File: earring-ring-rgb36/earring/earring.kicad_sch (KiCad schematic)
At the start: 44 parts, among them J1 Conn_01x04, SW1 SW_Push, U2 STM32L031G6Ux

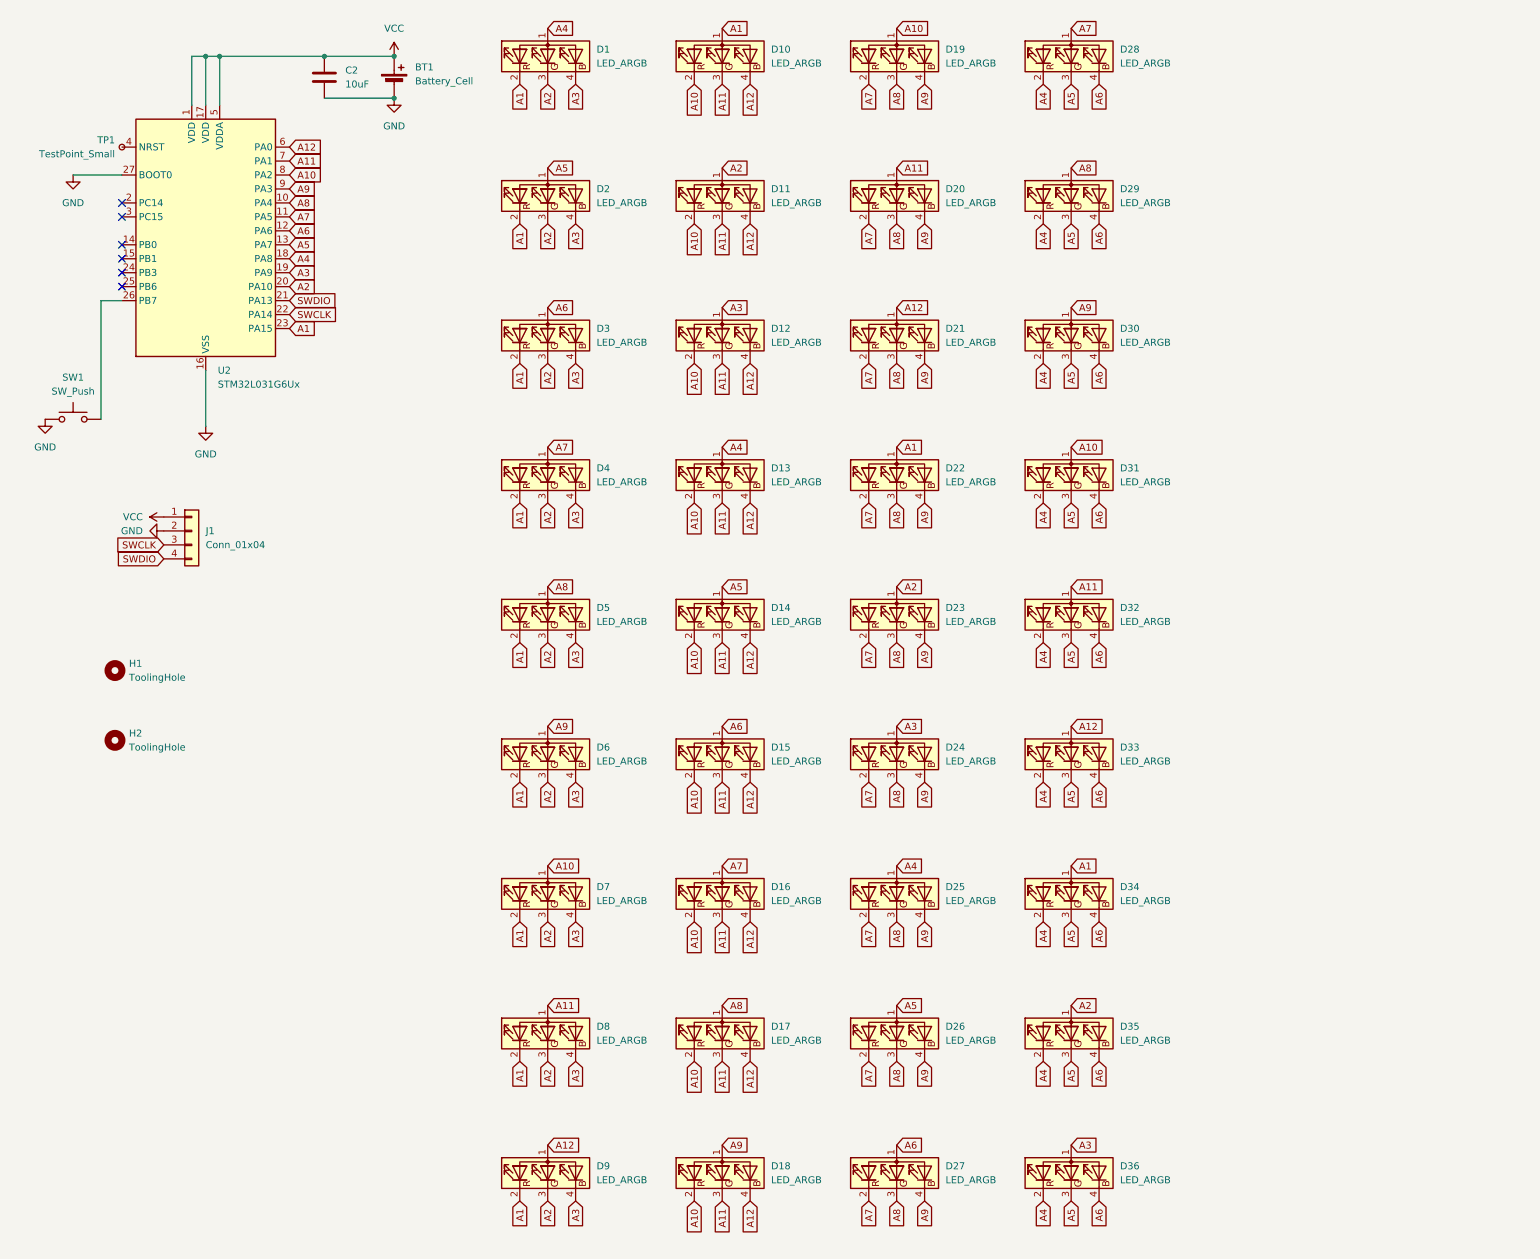
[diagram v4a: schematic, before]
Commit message: earring-ring-rgb36: updated PCB in many ways
 - updated to KiCad 9
 - added resistors for the LEDs (now assuming individual charlieplexing)
 - added MOSFET for reverse current protection
 - redid most of the wiring on the PCB, with the addition of the
   resistors
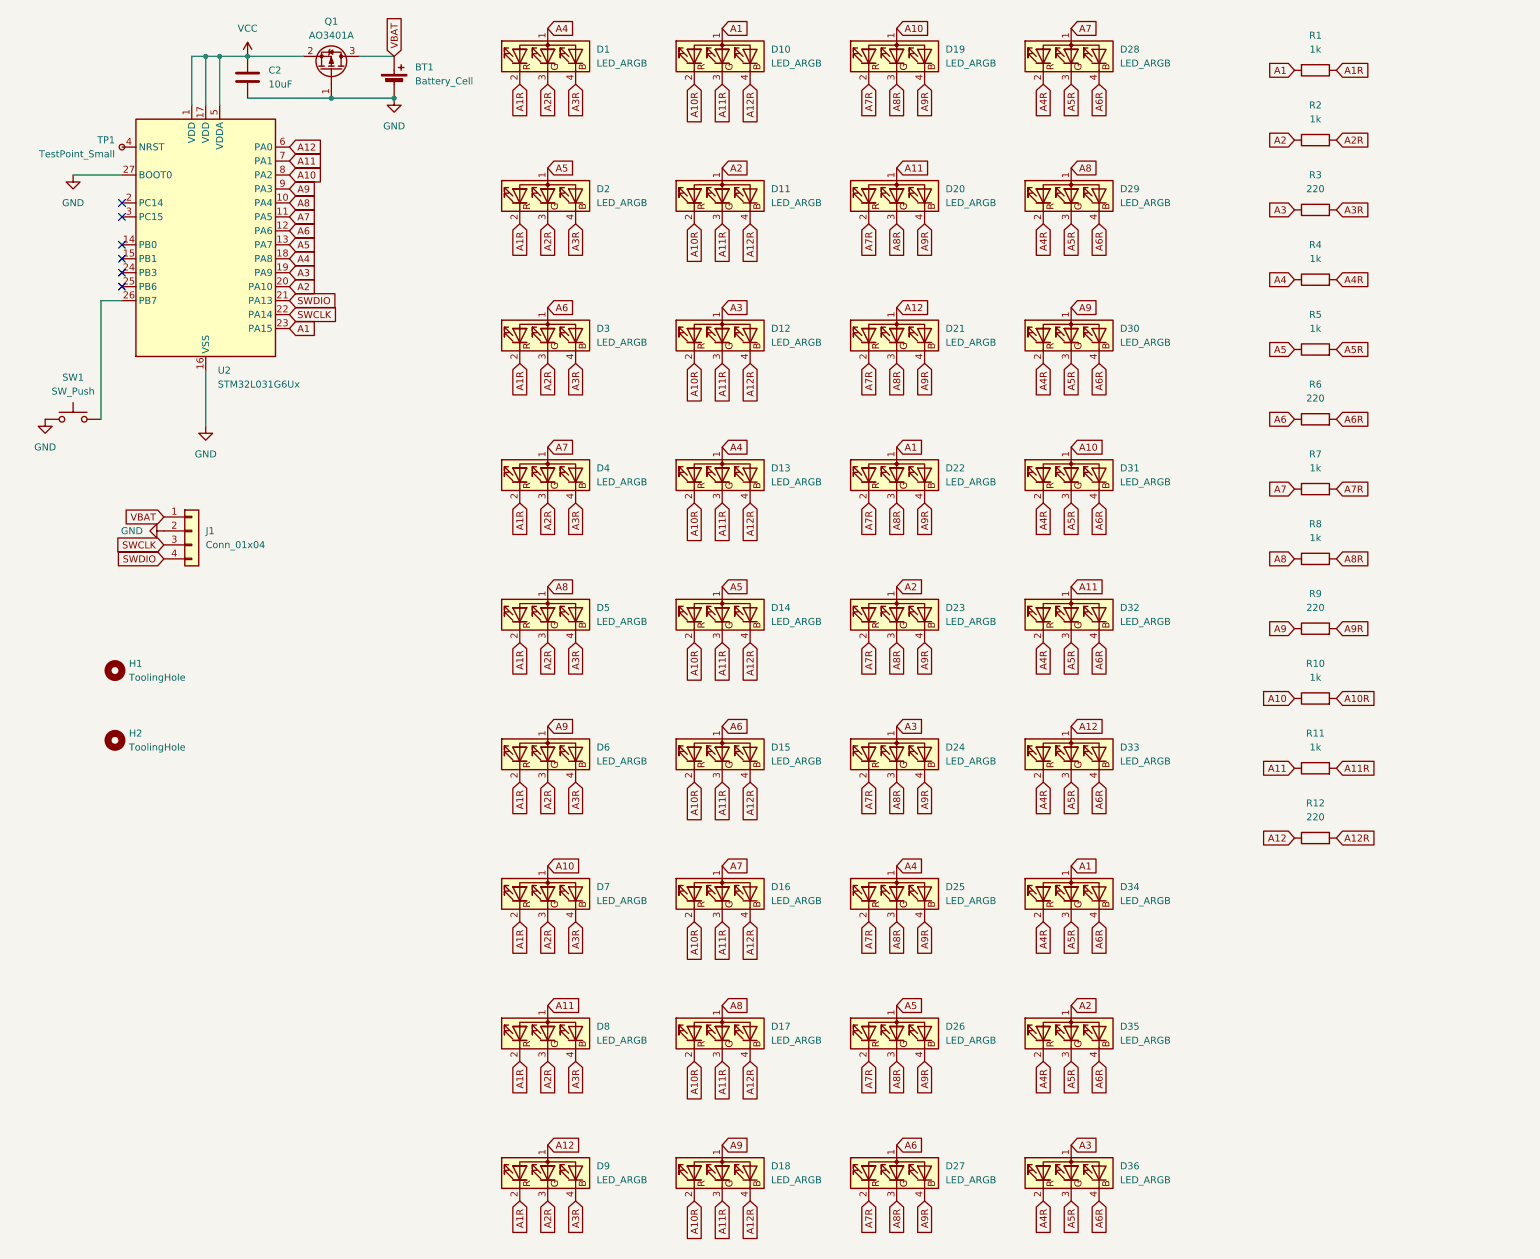
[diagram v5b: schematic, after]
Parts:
- added Q1: AO3401A, Package_TO_SOT_SMD:SOT-23, symbol Transistor_FET:AO3401A
- added R1, R10, R11, R2, R4, R5, R7, R8: 1k, Resistor_SMD:R_0402_1005Metric, symbol Device:R
- added R12, R3, R6, R9: 220, Resistor_SMD:R_0402_1005Metric, symbol Device:R
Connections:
- net A1: now also R1.2; no longer D1.2 (RK), D2.2 (RK), D3.2 (RK), D4.2 (RK), D5.2 (RK), D6.2 (RK), D7.2 (RK), D8.2 (RK), D9.2 (RK)
- net A10: now also R10.1; no longer D10.2 (RK), D11.2 (RK), D12.2 (RK), D13.2 (RK), D14.2 (RK), D15.2 (RK), D16.2 (RK), D17.2 (RK), D18.2 (RK)
- net A11: now also R11.1; no longer D10.3 (GK), D11.3 (GK), D12.3 (GK), D13.3 (GK), D14.3 (GK), D15.3 (GK), D16.3 (GK), D17.3 (GK), D18.3 (GK)
- net A12: now also R12.1; no longer D10.4 (BK), D11.4 (BK), D12.4 (BK), D13.4 (BK), D14.4 (BK), D15.4 (BK), D16.4 (BK), D17.4 (BK), D18.4 (BK)
- net A2: now also R2.1; no longer D1.3 (GK), D2.3 (GK), D3.3 (GK), D4.3 (GK), D5.3 (GK), D6.3 (GK), D7.3 (GK), D8.3 (GK), D9.3 (GK)
- net A3: now also R3.1; no longer D1.4 (BK), D2.4 (BK), D3.4 (BK), D4.4 (BK), D5.4 (BK), D6.4 (BK), D7.4 (BK), D8.4 (BK), D9.4 (BK)
- net A4: now also R4.1; no longer D28.2 (RK), D29.2 (RK), D30.2 (RK), D31.2 (RK), D32.2 (RK), D33.2 (RK), D34.2 (RK), D35.2 (RK), D36.2 (RK)
- net A5: now also R5.1; no longer D28.3 (GK), D29.3 (GK), D30.3 (GK), D31.3 (GK), D32.3 (GK), D33.3 (GK), D34.3 (GK), D35.3 (GK), D36.3 (GK)
- net A6: now also R6.1; no longer D28.4 (BK), D29.4 (BK), D30.4 (BK), D31.4 (BK), D32.4 (BK), D33.4 (BK), D34.4 (BK), D35.4 (BK), D36.4 (BK)
- net A7: now also R7.1; no longer D19.2 (RK), D20.2 (RK), D21.2 (RK), D22.2 (RK), D23.2 (RK), D24.2 (RK), D25.2 (RK), D26.2 (RK), D27.2 (RK)
- net A8: now also R8.1; no longer D19.3 (GK), D20.3 (GK), D21.3 (GK), D22.3 (GK), D23.3 (GK), D24.3 (GK), D25.3 (GK), D26.3 (GK), D27.3 (GK)
- net A9: now also R9.1; no longer D19.4 (BK), D20.4 (BK), D21.4 (BK), D22.4 (BK), D23.4 (BK), D24.4 (BK), D25.4 (BK), D26.4 (BK), D27.4 (BK)
- net GND: now also Q1.1 (G)
- net VCC: now also Q1.2 (S); no longer BT1.1 (+), J1.1 (Pin_1)
- new net A10R: D10.2 (RK), D11.2 (RK), D12.2 (RK), D13.2 (RK), D14.2 (RK), D15.2 (RK), D16.2 (RK), D17.2 (RK), D18.2 (RK), R10.2
- new net A11R: D10.3 (GK), D11.3 (GK), D12.3 (GK), D13.3 (GK), D14.3 (GK), D15.3 (GK), D16.3 (GK), D17.3 (GK), D18.3 (GK), R11.2
- new net A12R: D10.4 (BK), D11.4 (BK), D12.4 (BK), D13.4 (BK), D14.4 (BK), D15.4 (BK), D16.4 (BK), D17.4 (BK), D18.4 (BK), R12.2
- new net A1R: D1.2 (RK), D2.2 (RK), D3.2 (RK), D4.2 (RK), D5.2 (RK), D6.2 (RK), D7.2 (RK), D8.2 (RK), D9.2 (RK), R1.1
- new net A2R: D1.3 (GK), D2.3 (GK), D3.3 (GK), D4.3 (GK), D5.3 (GK), D6.3 (GK), D7.3 (GK), D8.3 (GK), D9.3 (GK), R2.2
- new net A3R: D1.4 (BK), D2.4 (BK), D3.4 (BK), D4.4 (BK), D5.4 (BK), D6.4 (BK), D7.4 (BK), D8.4 (BK), D9.4 (BK), R3.2
- new net A4R: D28.2 (RK), D29.2 (RK), D30.2 (RK), D31.2 (RK), D32.2 (RK), D33.2 (RK), D34.2 (RK), D35.2 (RK), D36.2 (RK), R4.2
- new net A5R: D28.3 (GK), D29.3 (GK), D30.3 (GK), D31.3 (GK), D32.3 (GK), D33.3 (GK), D34.3 (GK), D35.3 (GK), D36.3 (GK), R5.2
- new net A6R: D28.4 (BK), D29.4 (BK), D30.4 (BK), D31.4 (BK), D32.4 (BK), D33.4 (BK), D34.4 (BK), D35.4 (BK), D36.4 (BK), R6.2
- new net A7R: D19.2 (RK), D20.2 (RK), D21.2 (RK), D22.2 (RK), D23.2 (RK), D24.2 (RK), D25.2 (RK), D26.2 (RK), D27.2 (RK), R7.2
- new net A8R: D19.3 (GK), D20.3 (GK), D21.3 (GK), D22.3 (GK), D23.3 (GK), D24.3 (GK), D25.3 (GK), D26.3 (GK), D27.3 (GK), R8.2
- new net A9R: D19.4 (BK), D20.4 (BK), D21.4 (BK), D22.4 (BK), D23.4 (BK), D24.4 (BK), D25.4 (BK), D26.4 (BK), D27.4 (BK), R9.2
- new net VBAT: BT1.1 (+), J1.1 (Pin_1), Q1.3 (D)
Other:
- moved on the sheet: C2

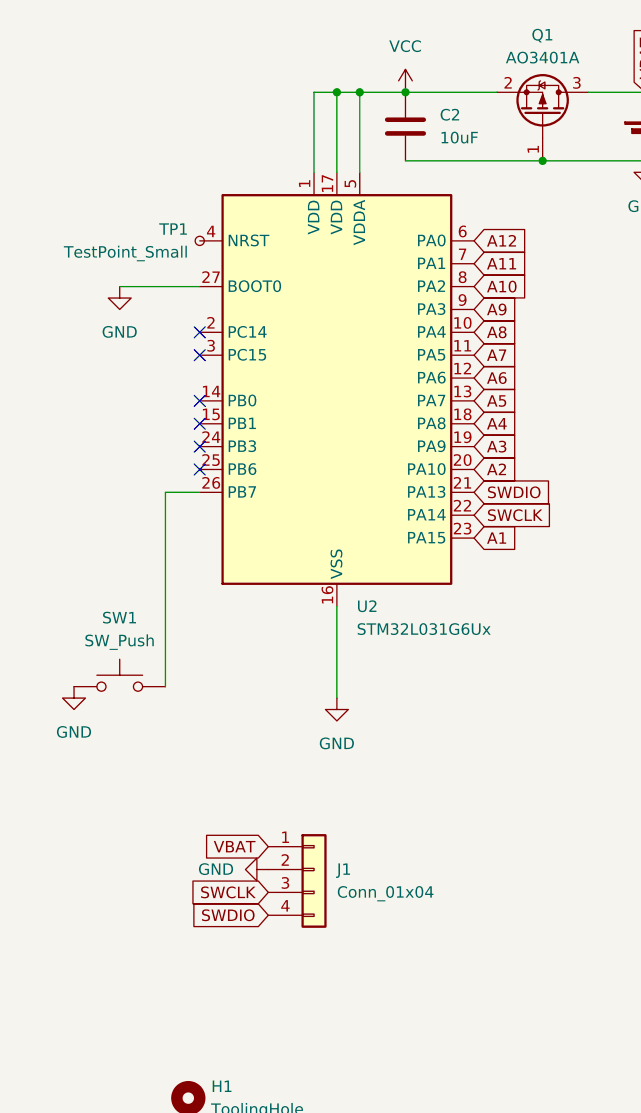
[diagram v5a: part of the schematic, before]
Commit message: earring-ring-rgb36: added reset pin to programming pins on the side
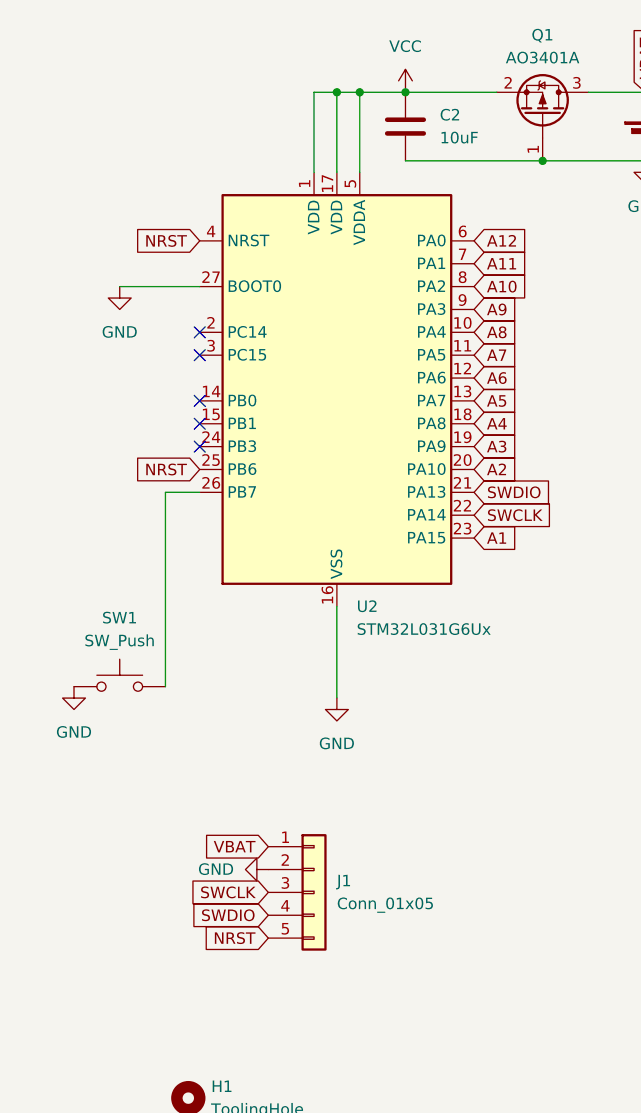
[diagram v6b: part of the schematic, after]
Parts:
- removed J1: Conn_01x04, Custom:ProgramHeader, symbol Connector_Generic:Conn_01x04
- removed TP1: TestPoint_Small, Custom:TestPoint_1.0x1.0mm, symbol Connector:TestPoint_Small
- added J1: Conn_01x05, Custom:ProgramHeader, symbol Connector_Generic:Conn_01x05
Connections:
- net GND: now also J1.2 (Pin_2)
- net SWCLK: now also J1.3 (Pin_3)
- net SWDIO: now also J1.4 (Pin_4)
- net VBAT: now also J1.1 (Pin_1)
- net NRST: now reaches U2.4 (NRST)
- net NRST: now also U2.25 (PB6), J1.5 (Pin_5)
- no-connect marks 6 -> 5
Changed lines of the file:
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@@
 	(paper "A3")
 	(junction
-		(at 43.18 22.86)
-		(diameter 0)
-		(color 0 0 0 0)
-	)
-	(junction
 		(at 66.04 30.48)
 		(diameter 0)
@@
 		(color 0 0 0 0)
 	)
-	(no_connect
-		(at 27.94 64.77)
+	(junction
+		(at 43.18 22.86)
+		(diameter 0)
+		(color 0 0 0 0)
 	)
 	(no_connect
@@
 	(wire
 		(pts
+			(xy 45.72 22.86) (xy 50.8 22.86)
+		)
+		(stroke
+			(width 0)
+			(type default)
+		)
+	)
+	(wire
+		(pts
 			(xy 45.72 31.75) (xy 45.72 22.86)
 		)
@@
 	(wire
 		(pts
-			(xy 45.72 22.86) (xy 43.18 22.86)
+			(xy 43.18 22.86) (xy 45.72 22.86)
 		)
 		(stroke
@@
 	(wire
 		(pts
-			(xy 45.72 22.86) (xy 50.8 22.86)
-		)
-		(stroke
-			(width 0)
-			(type default)
-		)
-	)
-	(wire
-		(pts
 			(xy 71.12 22.86) (xy 77.47 22.86)
 		)
@@
 	(wire
 		(pts
-			(xy 43.18 22.86) (xy 40.64 22.86)
+			(xy 40.64 22.86) (xy 43.18 22.86)
 		)
 		(stroke
@@
 		)
 	)
+	(global_label "NRST"
+		(shape input)
+		(at 27.94 64.77 180)
+		(fields_autoplaced yes)
+		(effects
+			(font
+				(size 1.27 1.27)
+			)
+			(justify right)
+		)
+		(property "Intersheetrefs" "${INTERSHEET_REFS}"
+			(at 20.1772 64.77 0)
+			(effects
+				(font
+					(size 1.27 1.27)
+				)
+				(justify right)
+				(hide yes)
+			)
+		)
+	)
 	(global_label "A1R"
 		(shape input)
@@
 		)
 	)
+	(global_label "NRST"
+		(shape input)
+		(at 27.94 39.37 180)
+		(fields_autoplaced yes)
+		(effects
+			(font
+				(size 1.27 1.27)
+			)
+			(justify right)
+		)
+		(property "Intersheetrefs" "${INTERSHEET_REFS}"
+			(at 20.1772 39.37 0)
+			(effects
+				(font
+					(size 1.27 1.27)
+				)
+				(justify right)
+				(hide yes)
+			)
+		)
+	)
 	(global_label "A11"
 		(shape input)
@@
 		)
 	)
+	(global_label "NRST"
+		(shape input)
+		(at 35.56 116.84 180)
+		(fields_autoplaced yes)
+		(effects
+			(font
+				(size 1.27 1.27)
+			)
+			(justify right)
+		)
+		(property "Intersheetrefs" "${INTERSHEET_REFS}"
+			(at 27.7972 116.84 0)
+			(effects
+				(font
+					(size 1.27 1.27)
+				)
+				(justify right)
+				(hide yes)
+			)
+		)
+	)
 	(global_label "A12R"
 		(shape input)
@@
 	)
 	(symbol
-		(lib_id "Connector:TestPoint_Small")
-		(at 27.94 39.37 0)
-		(mirror y)
-		(unit 1)
-		(exclude_from_sim no)
-		(in_bom no)
-		(on_board yes)
-		(dnp no)
-		(property "Reference" "TP1"
-			(at 26.67 38.0999 0)
-			(effects
-				(font
-					(size 1.27 1.27)
-				)
-				(justify left)
-			)
-		)
-		(property "Value" "TestPoint_Small"
-			(at 26.67 40.6399 0)
-			(effects
-				(font
-					(size 1.27 1.27)
-				)
-				(justify left)
-			)
-		)
-		(property "Footprint" "Custom:TestPoint_1.0x1.0mm"
-			(at 22.86 39.37 0)
-			(effects
-				(font
-					(size 1.27 1.27)
-				)
-				(hide yes)
-			)
-		)
-		(property "Datasheet" "~"
-			(at 22.86 39.37 0)
-			(effects
-				(font
-					(size 1.27 1.27)
-				)
-				(hide yes)
-			)
-		)
-		(property "Description" "test point"
-			(at 27.94 39.37 0)
-			(effects
-				(font
-					(size 1.27 1.27)
-				)
-				(hide yes)
-			)
-		)
-		(pin "1"
-		)
-		(instances
-			(project ""
-				(path "/5b672b97-2486-4be1-9927-7141d9b63fb2"
-					(reference "TP1")
-					(unit 1)
-				)
-			)
-		)
-	)
-	(symbol
 		(lib_id "Device:LED_ARGB")
 		(at 168.91 124.46 90)
@@
 	)
 	(symbol
-		(lib_id "Connector_Generic:Conn_01x04")
-		(at 40.64 109.22 0)
-		(unit 1)
-		(exclude_from_sim no)
-		(in_bom no)
-		(on_board yes)
-		(dnp no)
-		(fields_autoplaced yes)
-		(property "Reference" "J1"
-			(at 43.18 109.2199 0)
-			(effects
-				(font
-					(size 1.27 1.27)
-				)
-				(justify left)
-			)
-		)
-		(property "Value" "Conn_01x04"
-			(at 43.18 111.7599 0)
-			(effects
-				(font
-					(size 1.27 1.27)
-				)
-				(justify left)
-			)
-		)
-		(property "Footprint" "Custom:ProgramHeader"
-			(at 40.64 109.22 0)
-			(effects
-				(font
-					(size 1.27 1.27)
-				)
-				(hide yes)
-			)
-		)
-		(property "Datasheet" "~"
-			(at 40.64 109.22 0)
-			(effects
-				(font
-					(size 1.27 1.27)
-				)
-				(hide yes)
-			)
-		)
-		(property "Description" "Generic connector, single row, 01x04, script generated (kicad-library-utils/schlib/autogen/connector/)"
-			(at 40.64 109.22 0)
-			(effects
-				(font
-					(size 1.27 1.27)
-				)
-				(hide yes)
-			)
-		)
-		(pin "2"
-		)
-		(pin "4"
-		)
-		(pin "3"
-		)
-		(pin "1"
-		)
-		(instances
-			(project ""
-				(path "/5b672b97-2486-4be1-9927-7141d9b63fb2"
-					(reference "J1")
-					(unit 1)
-				)
-			)
-		)
-	)
-	(symbol
 		(lib_id "Device:LED_ARGB")
 		(at 137.16 149.86 90)
@@
 					(unit 1)
 				)
+			)
+		)
+	)
+	(symbol
+		(lib_id "Connector_Generic:Conn_01x05")
+		(at 40.64 111.76 0)
+		(unit 1)
+		(exclude_from_sim no)
+		(in_bom yes)
+		(on_board yes)
+		(dnp no)
+		(fields_autoplaced yes)
+		(property "Reference" "J1"
+			(at 43.18 110.4899 0)
+			(effects
+				(font
+					(size 1.27 1.27)
+				)
+				(justify left)
+			)
+		)
+		(property "Value" "Conn_01x05"
+			(at 43.18 113.0299 0)
+			(effects
+				(font
+					(size 1.27 1.27)
+				)
+				(justify left)
+			)
+		)
+		(property "Footprint" "Custom:ProgramHeader"
+			(at 40.64 111.76 0)
+			(effects
+				(font
+					(size 1.27 1.27)
+				)
+				(hide yes)
+			)
+		)
+		(property "Datasheet" "~"
+			(at 40.64 111.76 0)
+			(effects
+				(font
+					(size 1.27 1.27)
+				)
+				(hide yes)
+			)
+		)
+		(property "Description" "Generic connector, single row, 01x05, script generated (kicad-library-utils/schlib/autogen/connector/)"
+			(at 40.64 111.76 0)
+			(effects
+				(font
+					(size 1.27 1.27)
+				)
+				(hide yes)
+			)
+		)
+		(pin "4"
+		)
+		(pin "5"
+		)
+		(pin "2"
+		)
+		(pin "1"
+		)
+		(pin "3"
+		)
+		(instances
+			(project ""
+				(path "/5b672b97-2486-4be1-9927-7141d9b63fb2"
+					(reference "J1")
+					(unit 1)
+				)
